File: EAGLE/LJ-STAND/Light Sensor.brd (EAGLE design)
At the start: 119 x 119 mm, 122 parts

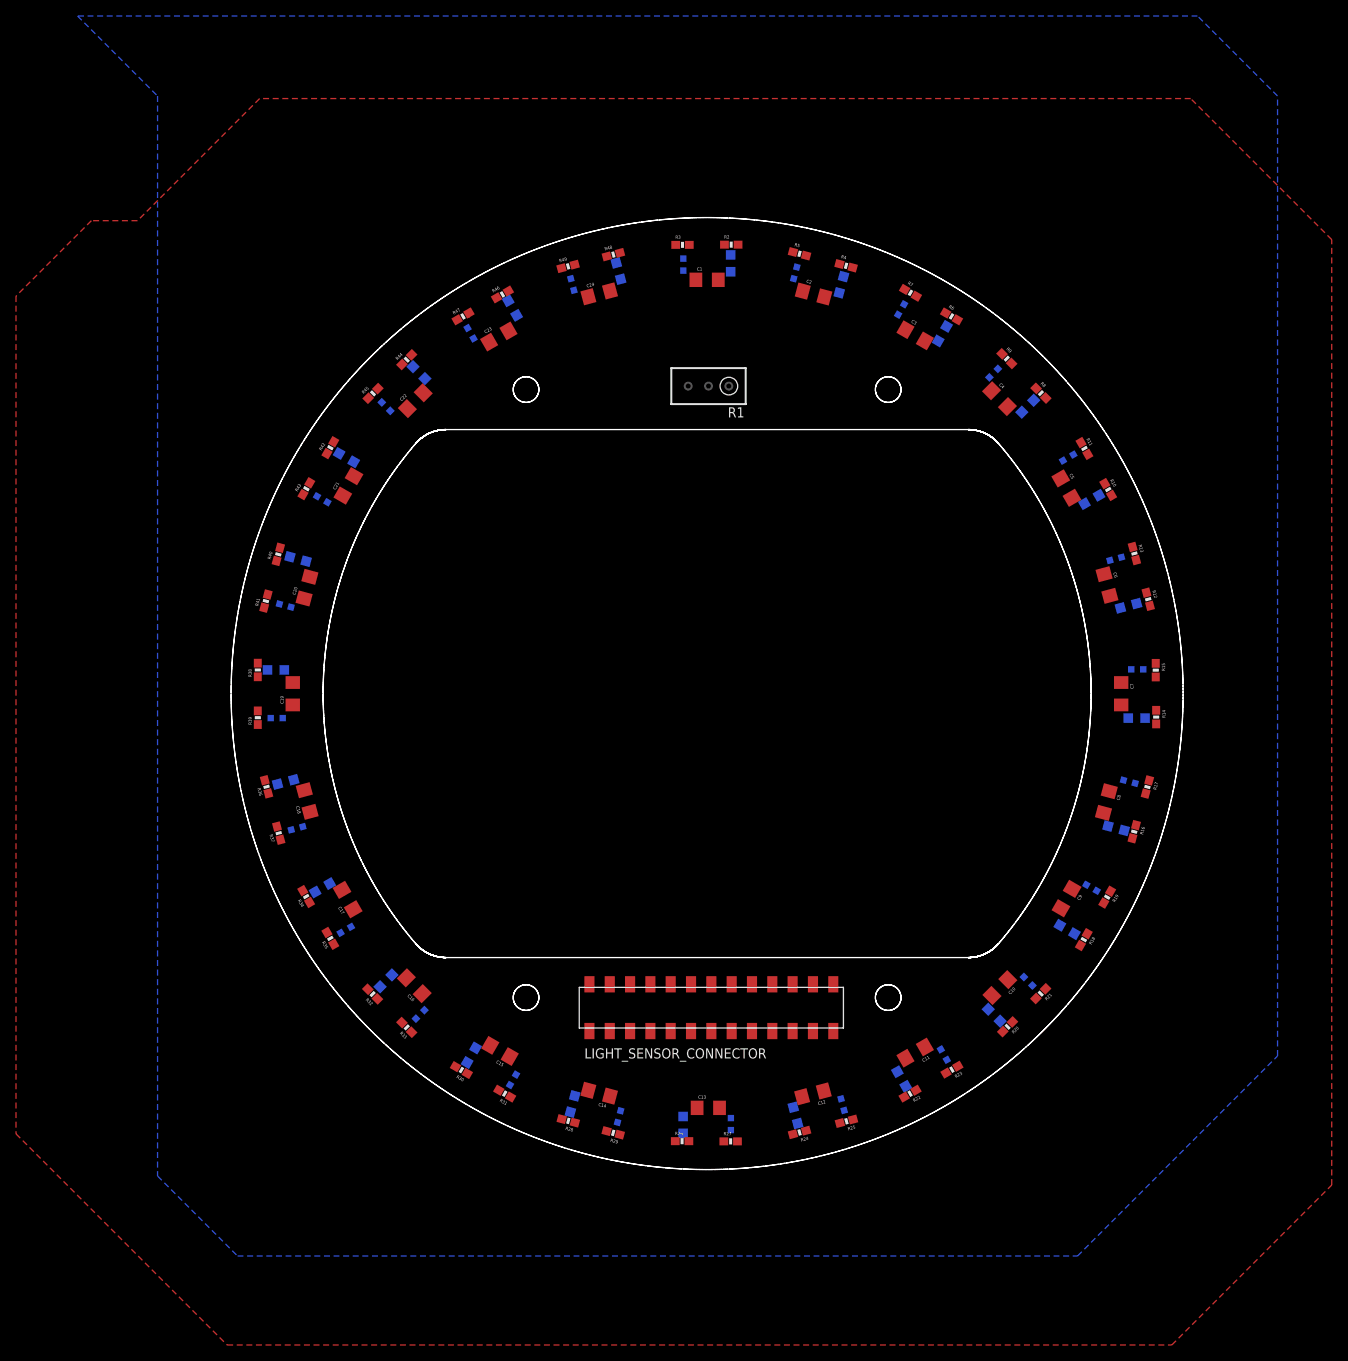
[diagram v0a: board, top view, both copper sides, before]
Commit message: Some traces on light
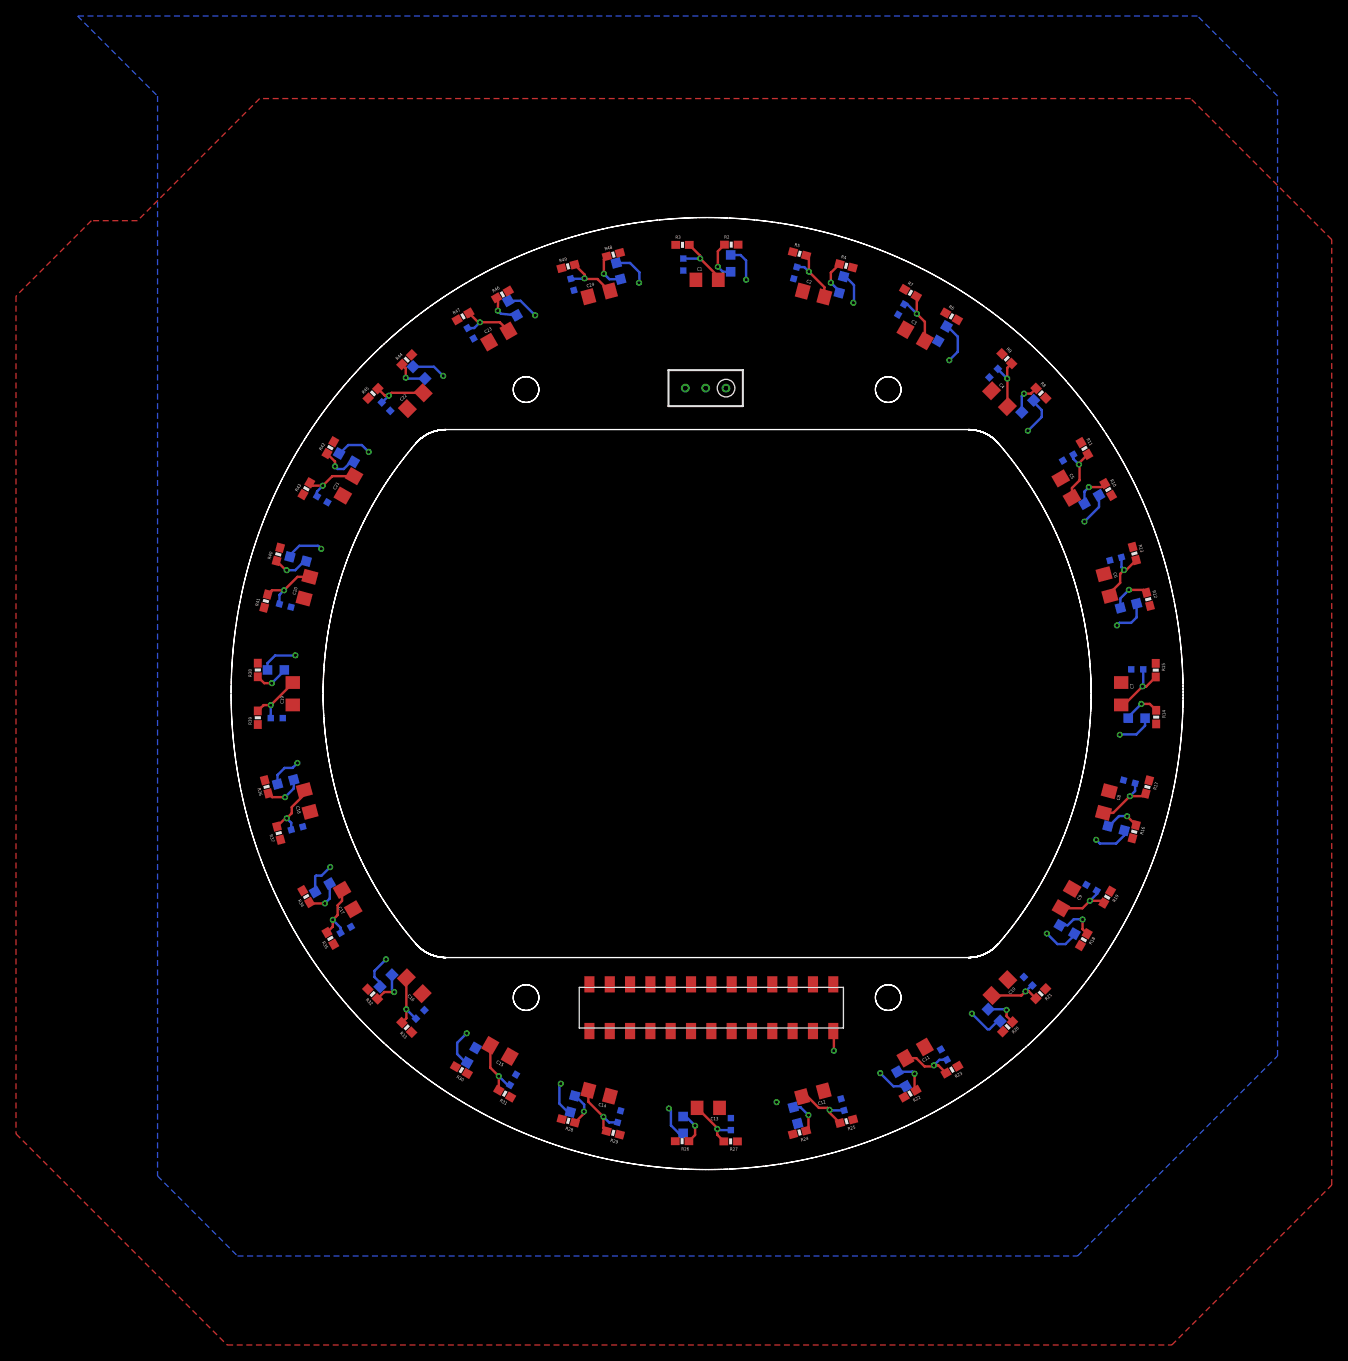
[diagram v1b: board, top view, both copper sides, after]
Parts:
- moved R1 0.44 mm to (148.5, 143.5)
- turned C13 to 180 degrees
- turned R26 to 180 degrees
- turned R27 to 180 degrees
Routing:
- net GND: track 0.00 -> 103.4 mm, vias 0 -> 24
- net LS7: track 0.00 -> 8.15 mm, vias 0 -> 1
- net LS11: track 0.00 -> 8.14 mm, vias 0 -> 1
- net LS19: track 0.00 -> 8.14 mm, vias 0 -> 1
- net LS16: track 0.00 -> 8.13 mm, vias 0 -> 1
- net LS2: track 0.00 -> 8.09 mm, vias 0 -> 1
- net LS13: track 0.00 -> 8.09 mm, vias 0 -> 1
- net LS0: track 0.05 -> 8.04 mm, vias 0 -> 1
- net LS6: track 0.00 -> 7.94 mm, vias 0 -> 1
- net LS14: track 0.00 -> 7.91 mm, vias 0 -> 1
- net LS1: track 0.00 -> 7.86 mm, vias 0 -> 1
- net LS10: track 0.00 -> 7.86 mm, vias 0 -> 1
- net LS4: track 0.00 -> 7.84 mm, vias 0 -> 1
- net LS20: track 0.00 -> 7.80 mm, vias 0 -> 1
- net LS23: track 0.00 -> 7.79 mm, vias 0 -> 1
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- added copper zone on layer 16, net +3V3
- added copper zone on layer 1, net GND
- removed copper zone on layer 1, net +3V3
- removed copper zone on layer 16, net GND

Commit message: More traces
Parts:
- moved LIGHT_SENSOR_CONNECTOR 1.22 mm to (148.8, 64.9), turned to 180 degrees
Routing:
- net LED_PWR: track 0.00 -> 402.1 mm
- net LS0: track 8.04 -> 201.3 mm, vias 1 -> 3
- net LS23: track 7.79 -> 192.4 mm, vias 1 -> 3
- net LS1: track 7.86 -> 181.3 mm, vias 1 -> 3
- net LS22: track 8.17 -> 175.5 mm, vias 1 -> 3
- net LS2: track 8.09 -> 168.1 mm, vias 1 -> 3
- net LS21: track 7.42 -> 148.9 mm, vias 1 -> 3
- net LS3: track 7.33 -> 148.3 mm, vias 1 -> 3
- net LS4: track 7.84 -> 137.8 mm, vias 1 -> 3
- net LS5: track 7.72 -> 89.9 mm, vias 1 -> 3
- net LS20: track 7.80 -> 86.0 mm, vias 1 -> 2
- net LS6: track 7.94 -> 83.4 mm
- net LS7: track 8.15 -> 68.9 mm, vias 1 -> 3
- net LS8: track 7.46 -> 63.7 mm, vias 1 -> 3
- net LS15: track 7.50 -> 52.2 mm
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
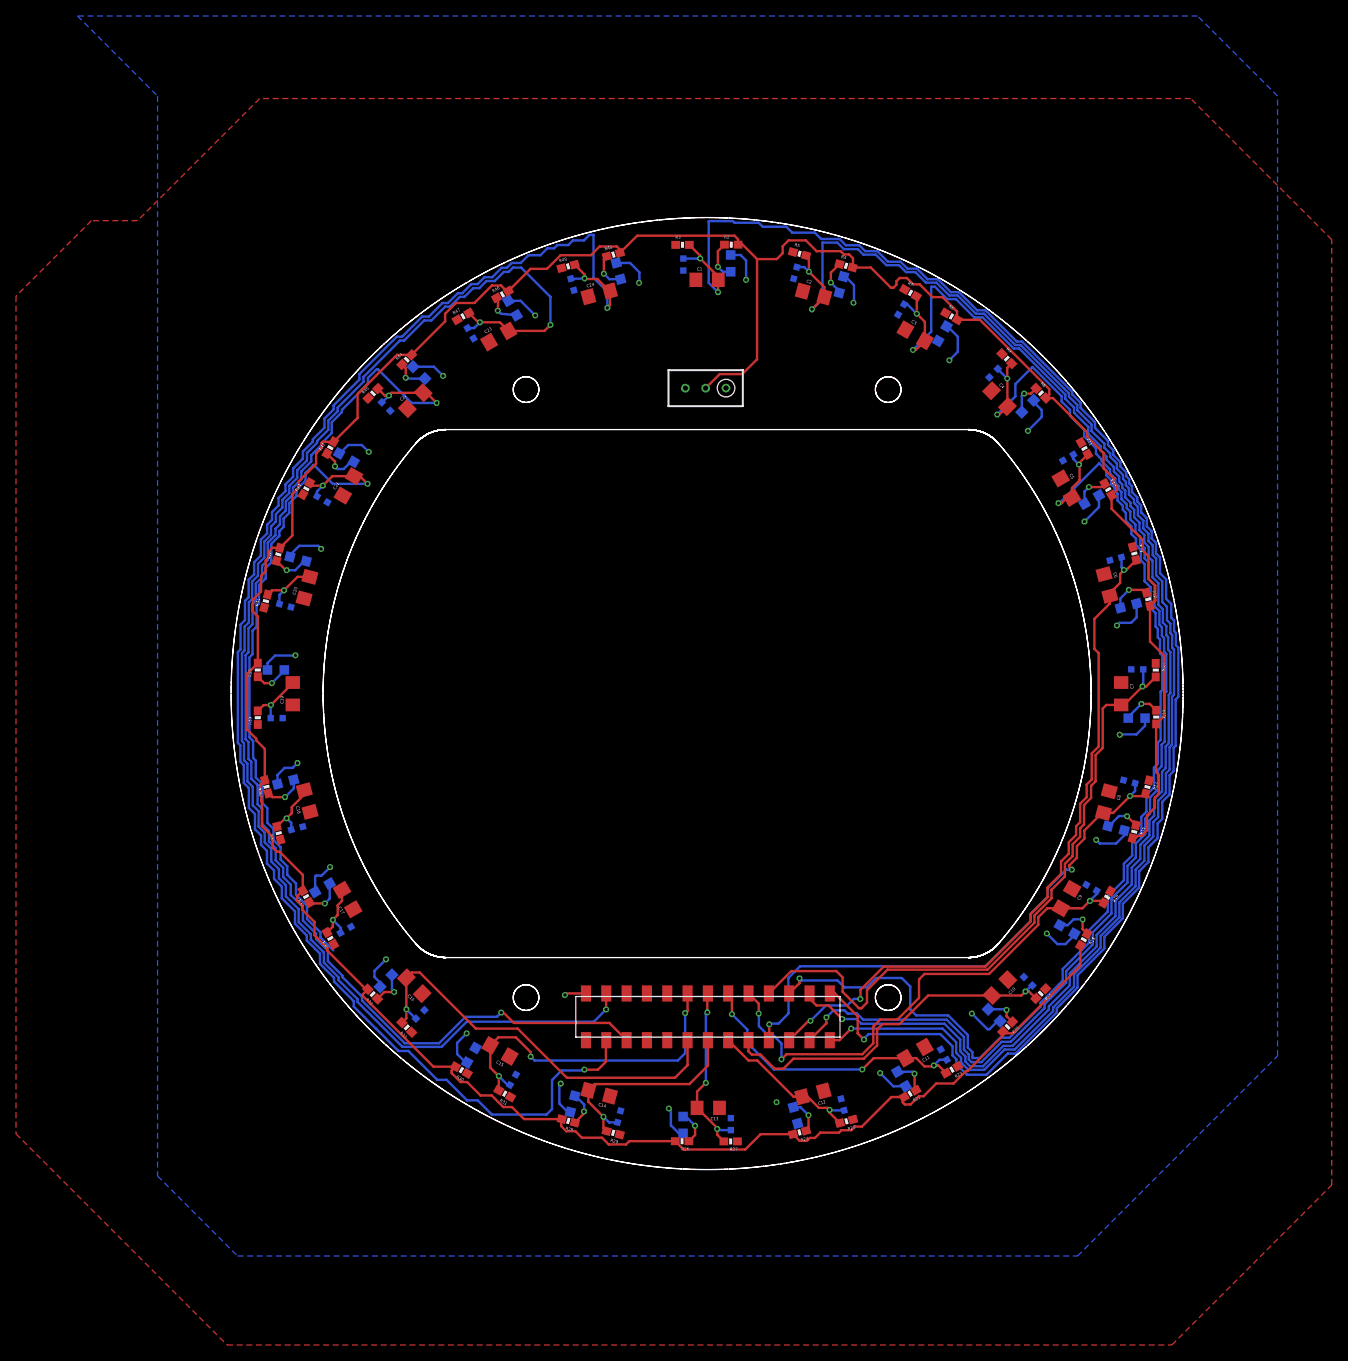
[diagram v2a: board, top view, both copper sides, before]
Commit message: finished light sensor pcb
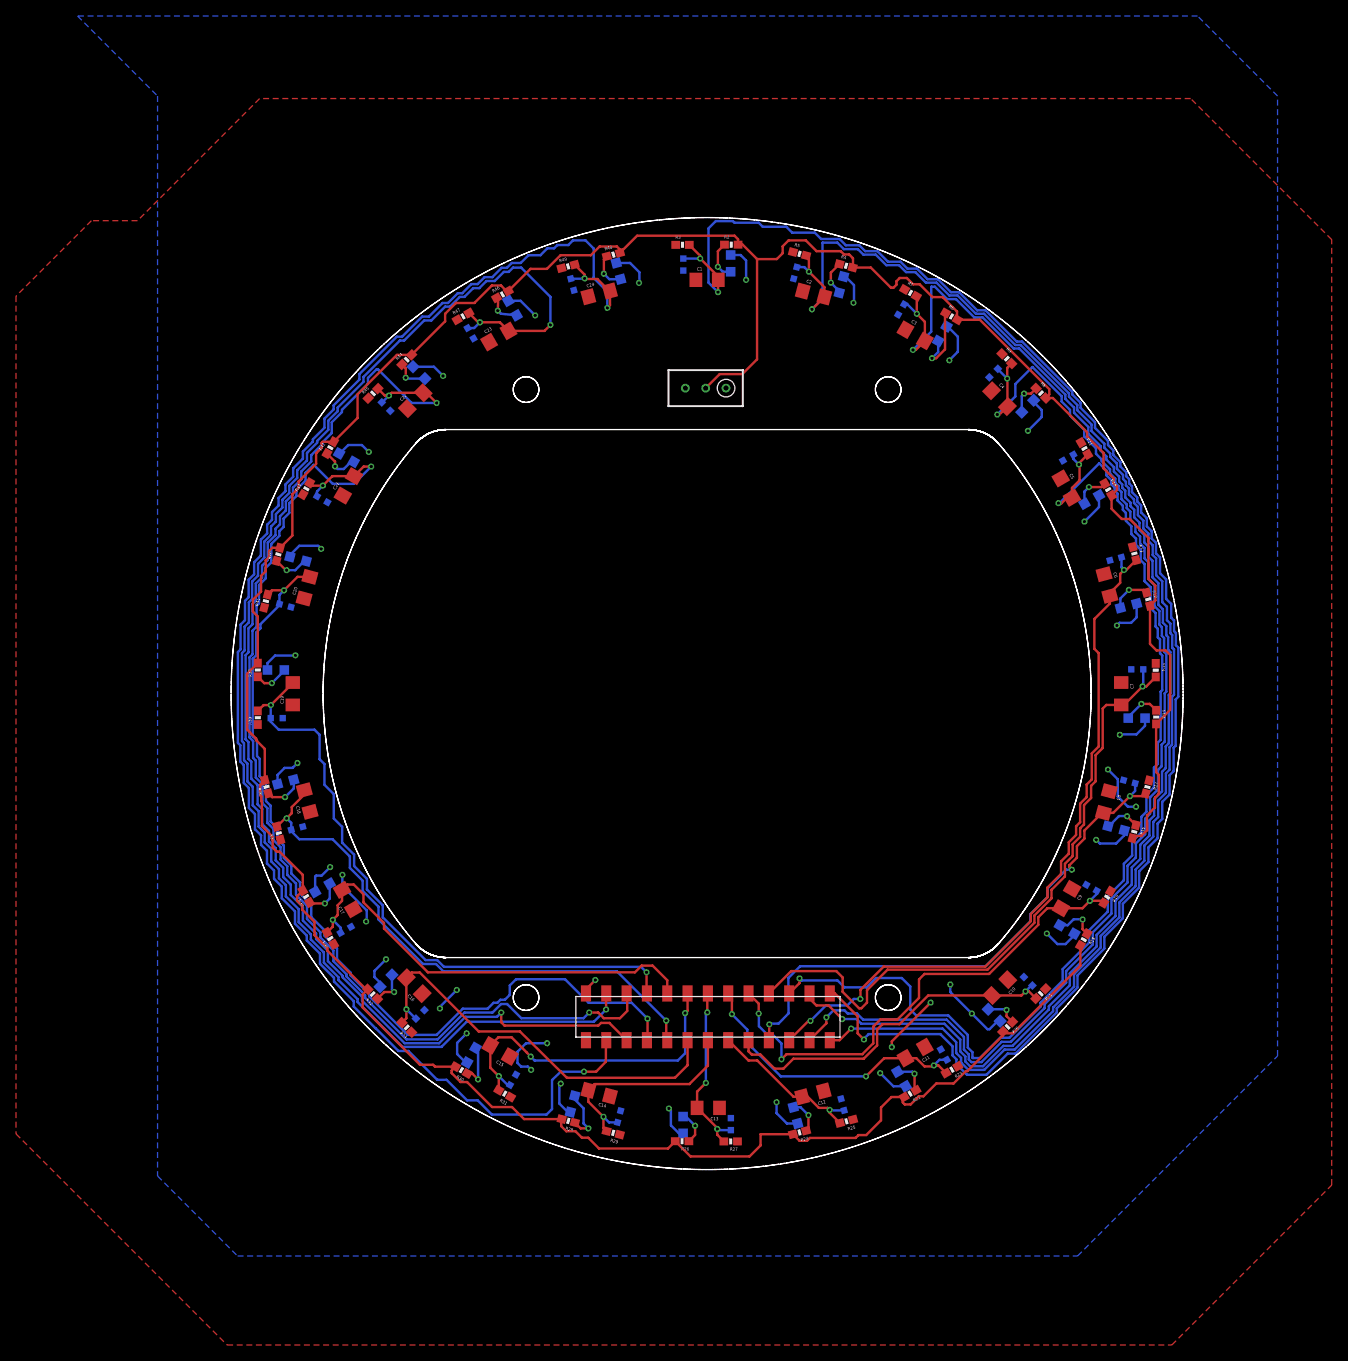
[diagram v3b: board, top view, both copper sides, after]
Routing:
- net LS19: track 8.14 -> 109.7 mm, vias 1 -> 2
- net LS18: track 7.52 -> 79.3 mm, vias 1 -> 2
- net LS17: track 7.74 -> 69.6 mm, vias 1 -> 2
- net LS20: track 86.0 -> 136.8 mm, vias 2 -> 3
- net LS16: track 8.13 -> 57.4 mm
- net GND: track 103.4 -> 137.3 mm, vias 24 -> 33
- net N$3: track 0.00 -> 9.14 mm, vias 0 -> 1
- net +3V3: track 2.73 -> 9.73 mm, vias 1 -> 3
- net N$15: track 0.00 -> 5.72 mm, vias 0 -> 1
- net LED_PWR: track 402.1 -> 407.7 mm
- net N$14: track 4.36 -> 6.76 mm
- net LS23: track 192.4 -> 190.8 mm
- net LS21: track 148.9 -> 149.9 mm
- net LS10: track 36.7 -> 37.5 mm
